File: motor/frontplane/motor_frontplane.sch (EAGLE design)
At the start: 28 parts, among them IC1 4001D, Q1 2N3904

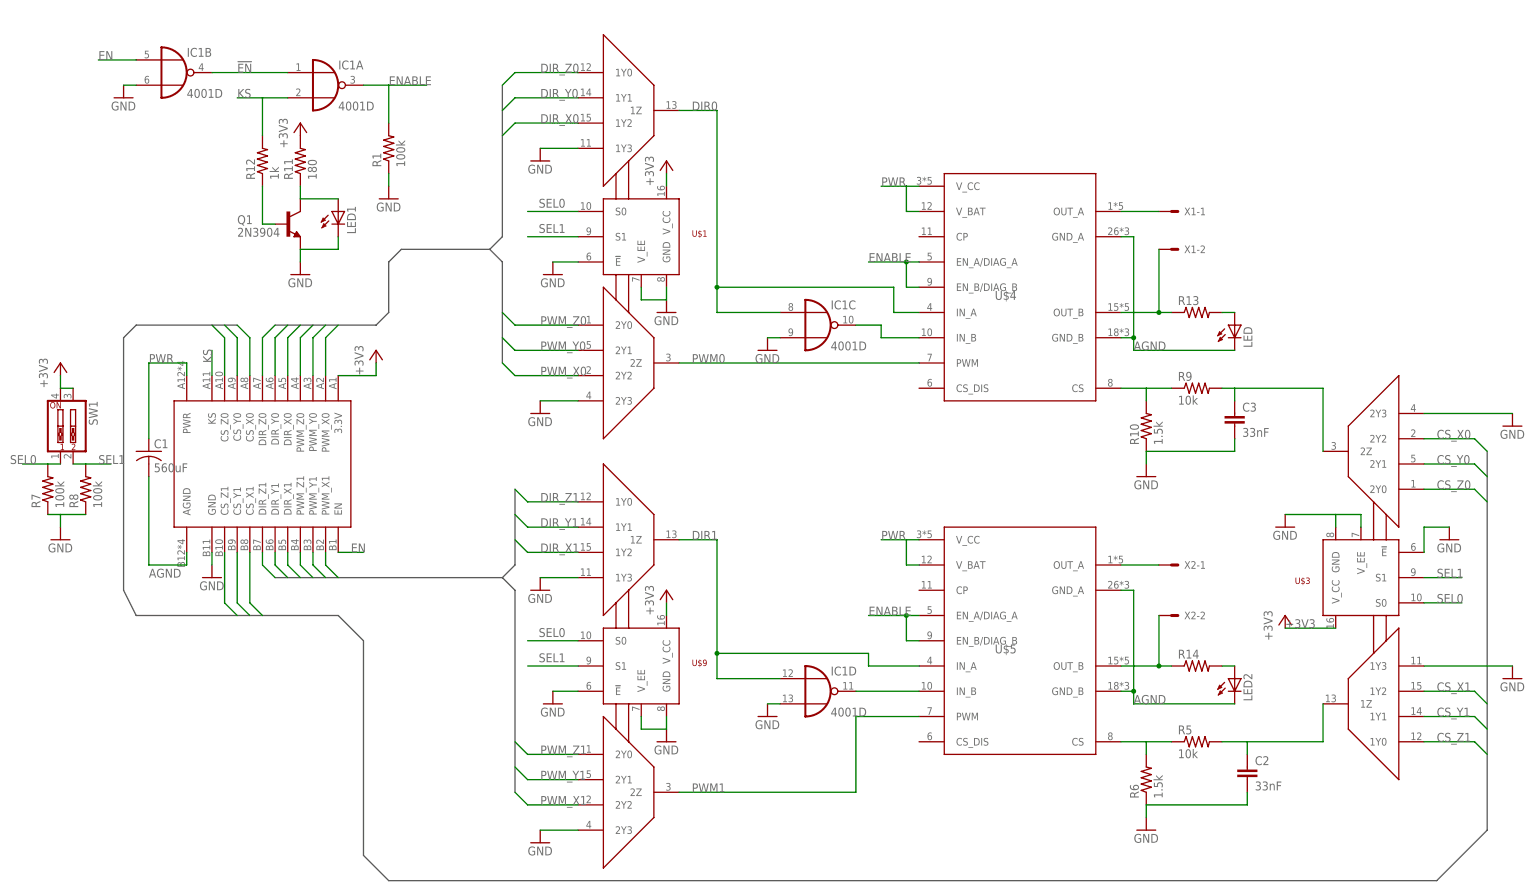
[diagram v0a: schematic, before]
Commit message: changed to NAND logic and produce draft PCB design
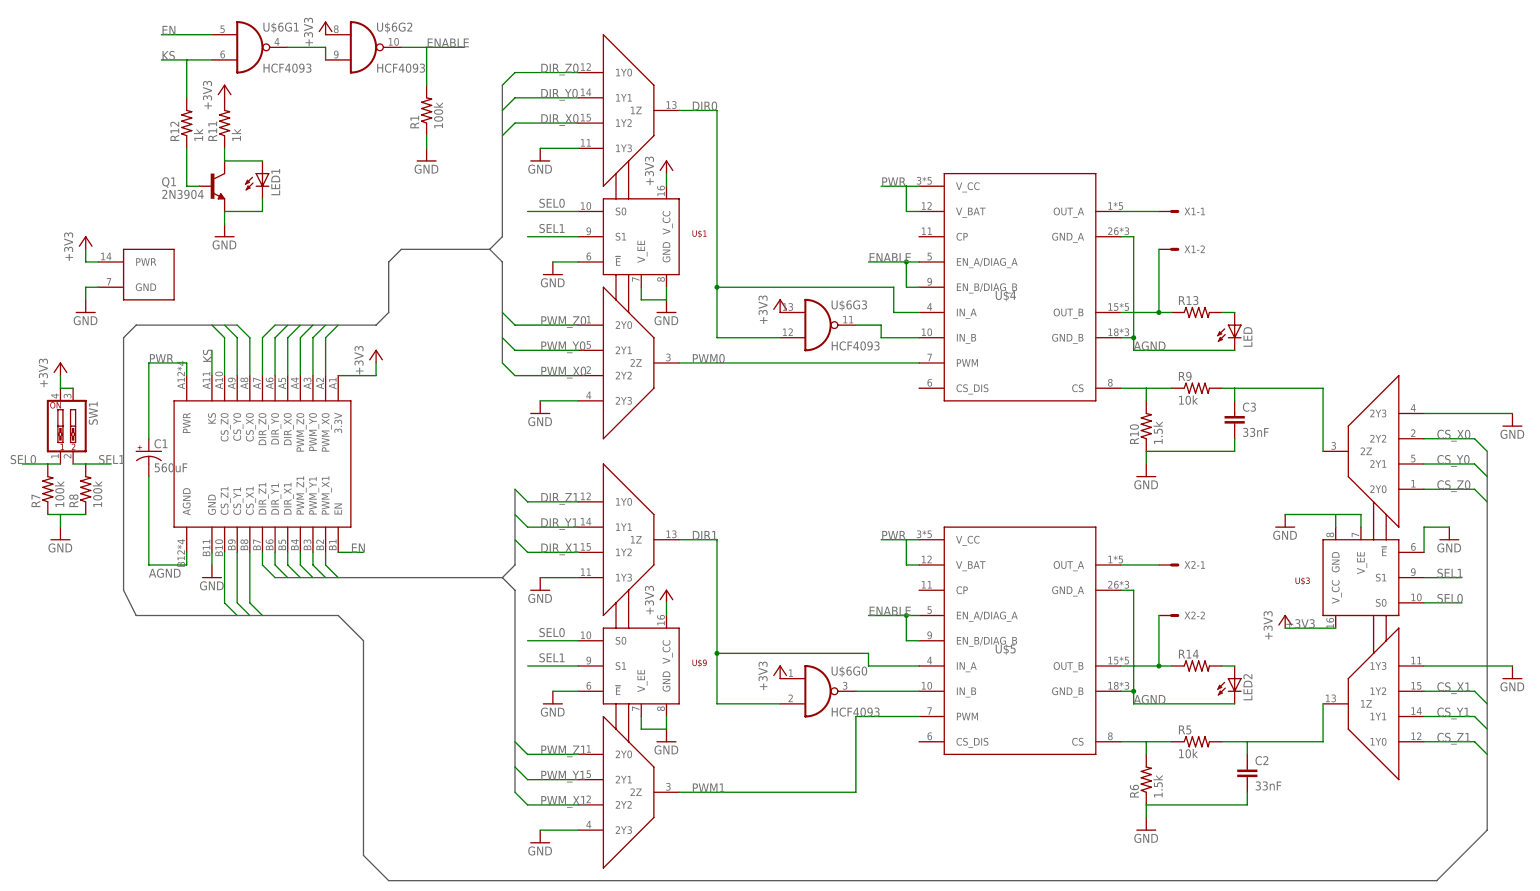
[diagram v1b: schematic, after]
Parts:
- removed IC1: 4001D, 40xx:4001D
- added U$6: HCF4093, ARVP:HCF4093
- C1: device resistor:C-US025-025X050 -> rcl:CPOL-USE3.5-10
- R11: value 180 -> 1k
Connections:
- net N$1 renamed OUT_A0
- net N$2 renamed OUT_B0
- net N$22 renamed CS1
- net N$3 renamed OUT_A1
- net N$4 renamed OUT_B1
- removed net !EN: IC1A.I0, IC1B.O
- removed net N$13: IC1C.O, U$4.IN_B
- removed net N$15: IC1D.O, U$5.IN_B
- removed net N$24: R10.2, R9.1
- new net !DIR0: U$4.IN_B, U$6G3.O
- new net !DIR1: U$5.IN_B, U$6G0.O
- new net CS0: R10.2, R9.1, U$4.CS
- new net N$5: U$6G1.O, U$6G2.I1
- net +3V3: now also U$6G$1.PWR, U$6G0.I0, U$6G2.I0, U$6G3.I0
- net AGND: now also C1.-; no longer C1.2
- net DIR0: now also U$6G3.I1; no longer IC1C.I0
- net DIR1: now also U$6G0.I1; no longer IC1D.I0
- net EN: no longer IC1B.I0
- net ENABLE: now also U$6G2.O; no longer IC1A.O
- net GND: now also U$6G$1.GND; no longer IC1B.I1, IC1C.I1, IC1D.I1
- net KS: now also U$6G1.I1; no longer IC1A.I1
- net PWR: now also C1.+; no longer C1.1
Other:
- moved on the sheet: LED1, Q1, R1, R11, R12

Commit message: changed sizing for the connectors
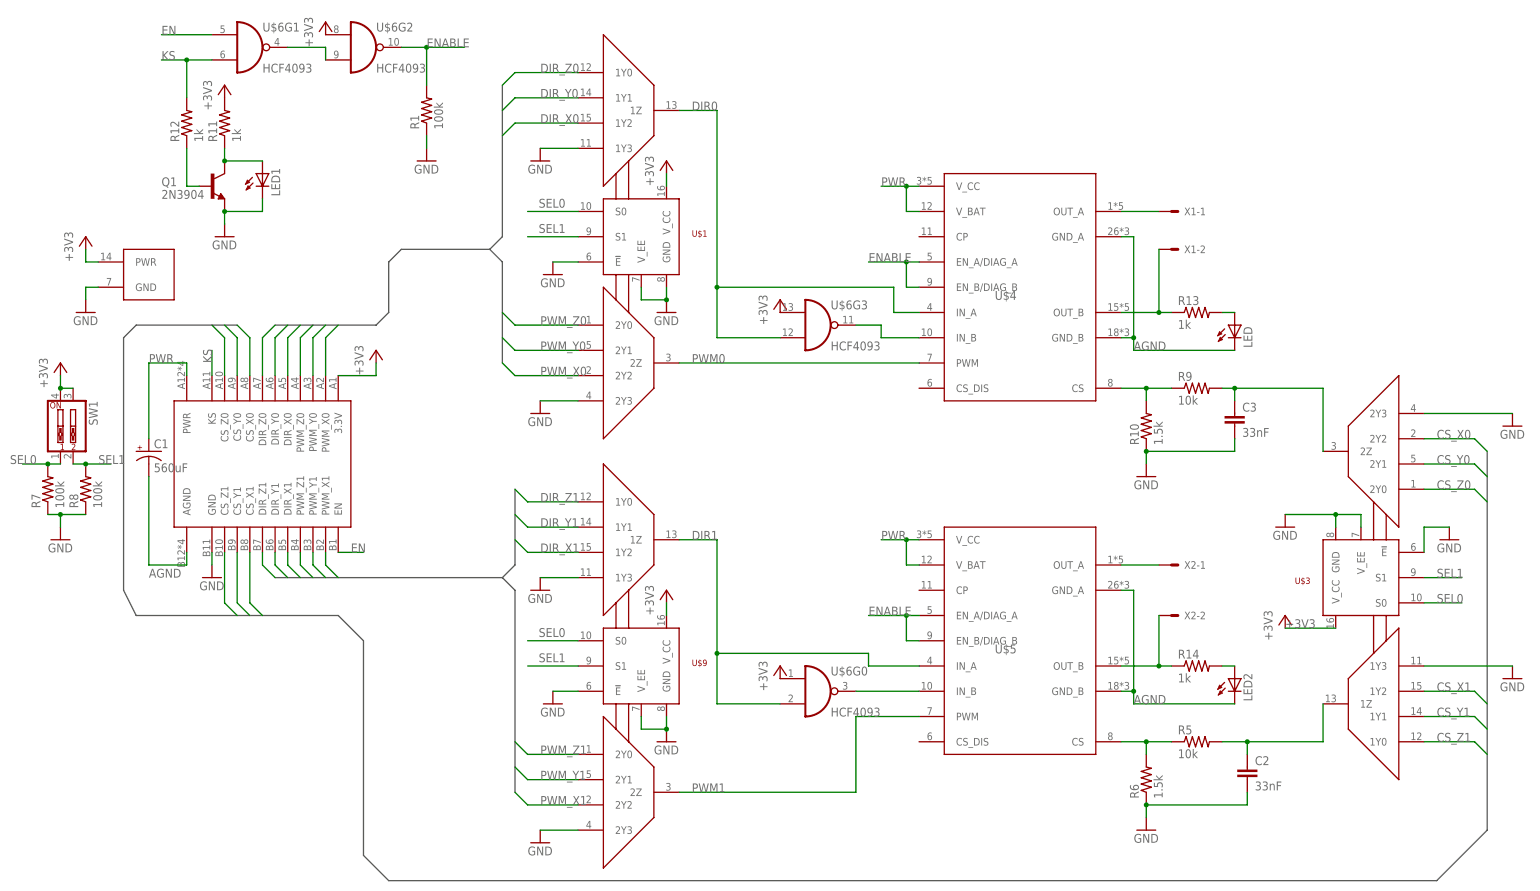
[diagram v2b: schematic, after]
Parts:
- R13, R14: value (none) -> 1k
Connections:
- removed net N$6: U$3.2Z
- net EN: now also U$6G1.I0
- net N$23: now also U$3.2Z
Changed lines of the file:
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@@
 <part name="GND18" library="supply1" deviceset="GND" device=""/>
 <part name="+3V9" library="supply1" deviceset="+3V3" device=""/>
-<part name="R13" library="rcl" deviceset="R-US_" device="R0805"/>
+<part name="R13" library="rcl" deviceset="R-US_" device="R0805" value="1k"/>
 <part name="LED" library="led" deviceset="LED" device="5MM"/>
-<part name="R14" library="rcl" deviceset="R-US_" device="R0805"/>
+<part name="R14" library="rcl" deviceset="R-US_" device="R0805" value="1k"/>
 <part name="LED2" library="led" deviceset="LED" device="5MM"/>
 <part name="U$2" library="ARVP" deviceset="MOTOR_BOARD_CONN" device=""/>
@@
 </instances>
 <busses>
-<bus name="B$1">
+<bus name="DIR_X1,DIR_Y1,DIR_Z1,PWM_X1,PWM_Y1,PWM_Z1">
 <segment>
 <wire x1="-86.36" y1="83.82" x2="-40.64" y2="83.82" width="0.762" layer="92"/>
@@
 </segment>
 </bus>
-<bus name="B$2">
+<bus name="DIR_X0,DIR_Y0,DIR_Z0,PWM_X0,PWM_Y0,PWM_Z0">
 <segment>
 <wire x1="-86.36" y1="134.62" x2="-66.04" y2="134.62" width="0.762" layer="92"/>
@@
 </segment>
 </bus>
-<bus name="B$3">
+<bus name="CS_X0,CS_X1,CS_Y0,CS_Y1,CS_Z0,CS_Z1">
 <segment>
 <wire x1="157.48" y1="109.22" x2="157.48" y2="33.02" width="0.762" layer="92"/>
@@
 <wire x1="40.64" y1="162.56" x2="35.56" y2="162.56" width="0.1524" layer="91"/>
 <label x="35.56" y="162.56" size="1.778" layer="95"/>
+<junction x="40.64" y="162.56"/>
 </segment>
 <segment>
@@
 <wire x1="40.64" y1="91.44" x2="35.56" y2="91.44" width="0.1524" layer="91"/>
 <label x="35.56" y="91.44" size="1.778" layer="95"/>
+<junction x="40.64" y="91.44"/>
 </segment>
 <segment>
@@
 </segment>
 </net>
-<net name="N$6" class="0">
-<segment>
-<pinref part="U$3" gate="G$1" pin="2Z"/>
-<wire x1="124.46" y1="121.92" x2="124.46" y2="109.22" width="0.1524" layer="91"/>
-</segment>
-</net>
 <net name="N$7" class="0">
 <segment>
@@
 <wire x1="109.22" y1="50.8" x2="124.46" y2="50.8" width="0.1524" layer="91"/>
 <wire x1="109.22" y1="48.26" x2="109.22" y2="50.8" width="0.1524" layer="91"/>
+<junction x="109.22" y="50.8"/>
 </segment>
 </net>
@@
 <wire x1="116.84" y1="96.52" x2="127" y2="96.52" width="0.1524" layer="91"/>
 <pinref part="GND5" gate="1" pin="GND"/>
+<junction x="127" y="96.52"/>
 </segment>
 <segment>
@@
 <wire x1="-7.62" y1="142.24" x2="-7.62" y2="139.7" width="0.1524" layer="91"/>
 <pinref part="GND7" gate="1" pin="GND"/>
+<junction x="-7.62" y="139.7"/>
 </segment>
 <segment>
@@
 <wire x1="-7.62" y1="55.88" x2="-7.62" y2="53.34" width="0.1524" layer="91"/>
 <pinref part="GND8" gate="1" pin="GND"/>
+<junction x="-7.62" y="53.34"/>
 </segment>
 <segment>
@@
 <wire x1="-129.54" y1="96.52" x2="-132.08" y2="96.52" width="0.1524" layer="91"/>
 <wire x1="-129.54" y1="93.98" x2="-129.54" y2="96.52" width="0.1524" layer="91"/>
+<junction x="-129.54" y="96.52"/>
 </segment>
 <segment>
@@
 <wire x1="109.22" y1="38.1" x2="88.9" y2="38.1" width="0.1524" layer="91"/>
 <wire x1="88.9" y1="38.1" x2="88.9" y2="35.56" width="0.1524" layer="91"/>
+<junction x="88.9" y="38.1"/>
 </segment>
 <segment>
@@
 <wire x1="88.9" y1="109.22" x2="106.68" y2="109.22" width="0.1524" layer="91"/>
 <wire x1="106.68" y1="109.22" x2="106.68" y2="111.76" width="0.1524" layer="91"/>
+<junction x="88.9" y="109.22"/>
 </segment>
 <segment>
@@
 <wire x1="-96.52" y1="157.48" x2="-96.52" y2="154.94" width="0.1524" layer="91"/>
 <pinref part="GND18" gate="1" pin="GND"/>
+<junction x="-96.52" y="157.48"/>
 </segment>
 <segment>
@@
 <wire x1="-104.14" y1="187.96" x2="-99.06" y2="187.96" width="0.1524" layer="91"/>
 <pinref part="U$6" gate="G1" pin="I1"/>
+<junction x="-104.14" y="187.96"/>
 </segment>
 <segment>
@@
 <pinref part="+3V8" gate="G$1" pin="+3V3"/>
 <wire x1="-129.54" y1="124.46" x2="-129.54" y2="121.92" width="0.1524" layer="91"/>
+<junction x="-129.54" y="121.92"/>
 </segment>
 <segment>
@@
 <wire x1="-124.46" y1="106.68" x2="-119.38" y2="106.68" width="0.1524" layer="91"/>
 <label x="-121.92" y="106.68" size="1.778" layer="95"/>
+<junction x="-124.46" y="106.68"/>
 </segment>
 </net>
@@
 <wire x1="-132.08" y1="106.68" x2="-137.16" y2="106.68" width="0.1524" layer="91"/>
 <label x="-139.7" y="106.68" size="1.778" layer="95"/>
+<junction x="-132.08" y="106.68"/>
 </segment>
 </net>
@@
 <wire x1="88.9" y1="50.8" x2="93.98" y2="50.8" width="0.1524" layer="91"/>
 <wire x1="88.9" y1="48.26" x2="88.9" y2="50.8" width="0.1524" layer="91"/>
+<junction x="88.9" y="50.8"/>
 </segment>
 </net>
@@
 <wire x1="104.14" y1="121.92" x2="106.68" y2="121.92" width="0.1524" layer="91"/>
 <pinref part="C3" gate="G$1" pin="1"/>
+<wire x1="106.68" y1="119.38" x2="106.68" y2="121.92" width="0.1524" layer="91"/>
+<pinref part="U$3" gate="G$1" pin="2Z"/>
 <wire x1="106.68" y1="121.92" x2="124.46" y2="121.92" width="0.1524" layer="91"/>
-<wire x1="106.68" y1="119.38" x2="106.68" y2="121.92" width="0.1524" layer="91"/>
+<wire x1="124.46" y1="121.92" x2="124.46" y2="109.22" width="0.1524" layer="91"/>
+<junction x="106.68" y="121.92"/>
 </segment>
 </net>
@@
 <pinref part="U$4" gate="G$1" pin="CS"/>
 <wire x1="83.82" y1="121.92" x2="88.9" y2="121.92" width="0.1524" layer="91"/>
+<junction x="88.9" y="121.92"/>
 </segment>
 </net>
@@
 <pinref part="R11" gate="G$1" pin="1"/>
 <wire x1="-96.52" y1="167.64" x2="-96.52" y2="170.18" width="0.1524" layer="91"/>
+<junction x="-96.52" y="167.64"/>
 </segment>
 </net>
@@
 <wire x1="-99.06" y1="193.04" x2="-109.22" y2="193.04" width="0.1524" layer="91"/>
 <label x="-109.22" y="193.04" size="1.778" layer="95"/>
+<pinref part="U$6" gate="G1" pin="I0"/>
 </segment>
 <segment>
@@
 <pinref part="U$6" gate="G2" pin="O"/>
 <wire x1="-60.96" y1="190.5" x2="-55.88" y2="190.5" width="0.1524" layer="91"/>
-</segment>
-</net>
+<junction x="-55.88" y="190.5"/>
+</segment>
+</net>
